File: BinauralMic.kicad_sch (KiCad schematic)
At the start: 0 parts

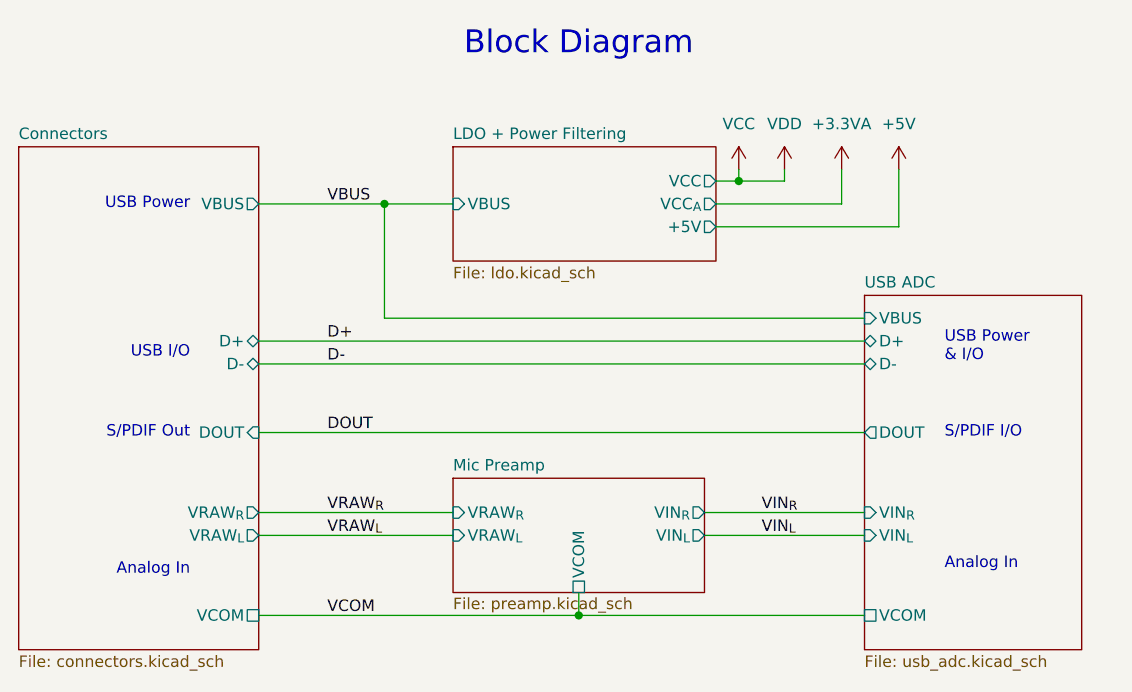
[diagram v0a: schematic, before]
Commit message: Redid schematic and component values according to new recalculations
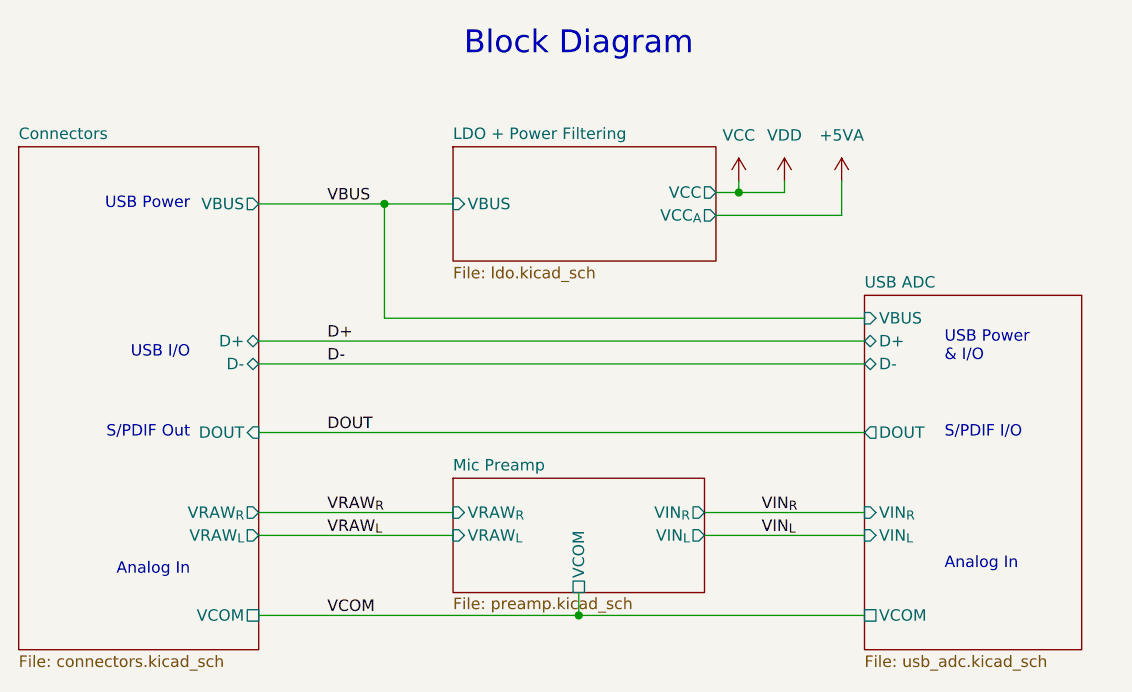
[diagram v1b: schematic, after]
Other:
- sheet LDO + Power Filtering ports: added none; removed +5V
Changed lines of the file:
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@@
 	(title_block
 		(title "Binaural Mic (Block Diagram)")
-		(date "2024-09-15")
-		(rev "1")
+		(date "2025-07-06")
+		(rev "2")
 		(company "Tachyon PCBAs")
-		(comment 1 "first try surely")
+		(comment 1 "second try surely")
 	)
 	(text "Analog In"
@@
 	)
 	(junction
-		(at 121.92 41.91)
+		(at 121.92 43.18)
 		(diameter 0)
 		(color 0 0 0 0)
@@
 	(wire
 		(pts
-			(xy 119.38 44.45) (xy 133.35 44.45)
+			(xy 119.38 45.72) (xy 133.35 45.72)
 		)
 		(stroke
@@
 	(wire
 		(pts
-			(xy 121.92 41.91) (xy 119.38 41.91)
-		)
-		(stroke
-			(width 0)
-			(type default)
-		)
-	)
-	(wire
-		(pts
-			(xy 127 41.91) (xy 121.92 41.91)
+			(xy 121.92 43.18) (xy 119.38 43.18)
+		)
+		(stroke
+			(width 0)
+			(type default)
+		)
+	)
+	(wire
+		(pts
+			(xy 127 43.18) (xy 121.92 43.18)
 		)
 		(stroke
@@
 	(wire
 		(pts
-			(xy 127 40.64) (xy 127 41.91)
+			(xy 127 41.91) (xy 127 43.18)
 		)
 		(stroke
@@
 	(wire
 		(pts
-			(xy 133.35 40.64) (xy 133.35 44.45)
+			(xy 133.35 41.91) (xy 133.35 45.72)
 		)
 		(stroke
@@
 	(wire
 		(pts
-			(xy 139.7 46.99) (xy 119.38 46.99)
-		)
-		(stroke
-			(width 0)
-			(type default)
-		)
-	)
-	(wire
-		(pts
 			(xy 82.55 44.45) (xy 90.17 44.45)
 		)
@@
 	(wire
 		(pts
-			(xy 139.7 40.64) (xy 139.7 46.99)
-		)
-		(stroke
-			(width 0)
-			(type default)
-		)
-	)
-	(wire
-		(pts
-			(xy 121.92 40.64) (xy 121.92 41.91)
+			(xy 121.92 41.91) (xy 121.92 43.18)
 		)
 		(stroke
@@
 	(symbol
 		(lib_id "power:VDD")
-		(at 127 40.64 0)
+		(at 127 41.91 0)
 		(mirror y)
 		(unit 1)
@@
 		(dnp no)
 		(property "Reference" "#PWR02"
-			(at 127 44.45 0)
+			(at 127 45.72 0)
 			(effects
 				(font
@@
 		)
 		(property "Value" "VDD"
-			(at 127 35.56 0)
+			(at 127 36.83 0)
 			(effects
 				(font
@@
 		)
 		(property "Footprint" ""
-			(at 127 40.64 0)
+			(at 127 41.91 0)
 			(effects
 				(font
@@
 		)
 		(property "Datasheet" ""
-			(at 127 40.64 0)
+			(at 127 41.91 0)
 			(effects
 				(font
@@
 		)
 		(property "Description" "Power symbol creates a global label with name \"VDD\""
-			(at 127 40.64 0)
+			(at 127 41.91 0)
 			(effects
 				(font
@@
 	)
 	(symbol
-		(lib_id "power:+3.3VA")
-		(at 133.35 40.64 0)
-		(unit 1)
-		(exclude_from_sim no)
-		(in_bom yes)
-		(on_board yes)
-		(dnp no)
-		(fields_autoplaced yes)
-		(property "Reference" "#PWR031"
-			(at 133.35 44.45 0)
-			(effects
-				(font
-					(size 1.27 1.27)
-				)
-				(hide yes)
-			)
-		)
-		(property "Value" "+3.3VA"
-			(at 133.35 35.56 0)
-			(effects
-				(font
-					(size 1.27 1.27)
-				)
-			)
-		)
-		(property "Footprint" ""
-			(at 133.35 40.64 0)
-			(effects
-				(font
-					(size 1.27 1.27)
-				)
-				(hide yes)
-			)
-		)
-		(property "Datasheet" ""
-			(at 133.35 40.64 0)
-			(effects
-				(font
-					(size 1.27 1.27)
-				)
-				(hide yes)
-			)
-		)
-		(property "Description" "Power symbol creates a global label with name \"+3.3VA\""
-			(at 133.35 40.64 0)
-			(effects
-				(font
-					(size 1.27 1.27)
-				)
-				(hide yes)
-			)
-		)
-		(pin "1"
-		)
-		(instances
-			(project "BinauralMic"
-				(path "/d9e790b9-8aa4-4e58-8bd7-6ef4bc890627"
-					(reference "#PWR031")
-					(unit 1)
-				)
-			)
-		)
-	)
-	(symbol
-		(lib_id "power:+5V")
-		(at 139.7 40.64 0)
+		(lib_id "power:+5VA")
+		(at 133.35 41.91 0)
 		(unit 1)
 		(exclude_from_sim no)
@@
 		(fields_autoplaced yes)
 		(property "Reference" "#PWR03"
-			(at 139.7 44.45 0)
-			(effects
-				(font
-					(size 1.27 1.27)
-				)
-				(hide yes)
-			)
-		)
-		(property "Value" "+5V"
-			(at 139.7 35.56 0)
+			(at 133.35 45.72 0)
+			(effects
+				(font
+					(size 1.27 1.27)
+				)
+				(hide yes)
+			)
+		)
+		(property "Value" "+5VA"
+			(at 133.35 36.83 0)
 			(effects
 				(font
@@
 		)
 		(property "Footprint" ""
-			(at 139.7 40.64 0)
+			(at 133.35 41.91 0)
 			(effects
 				(font
@@
 		)
 		(property "Datasheet" ""
-			(at 139.7 40.64 0)
-			(effects
-				(font
-					(size 1.27 1.27)
-				)
-				(hide yes)
-			)
-		)
-		(property "Description" "Power symbol creates a global label with name \"+5V\""
-			(at 139.7 40.64 0)
+			(at 133.35 41.91 0)
+			(effects
+				(font
+					(size 1.27 1.27)
+				)
+				(hide yes)
+			)
+		)
+		(property "Description" "Power symbol creates a global label with name \"+5VA\""
+			(at 133.35 41.91 0)
 			(effects
 				(font
@@
 		)
 		(instances
-			(project "BinauralMic"
+			(project ""
 				(path "/d9e790b9-8aa4-4e58-8bd7-6ef4bc890627"
 					(reference "#PWR03")
@@
 	(symbol
 		(lib_id "power:VCC")
-		(at 121.92 40.64 0)
+		(at 121.92 41.91 0)
 		(unit 1)
 		(exclude_from_sim no)
@@
 		(fields_autoplaced yes)
 		(property "Reference" "#PWR01"
-			(at 121.92 44.45 0)
+			(at 121.92 45.72 0)
 			(effects
 				(font
@@
 		)
 		(property "Value" "VCC"
-			(at 121.92 35.56 0)
+			(at 121.92 36.83 0)
 			(effects
 				(font
@@
 		)
 		(property "Footprint" ""
-			(at 121.92 40.64 0)
+			(at 121.92 41.91 0)
 			(effects
 				(font
@@
 		)
 		(property "Datasheet" ""
-			(at 121.92 40.64 0)
+			(at 121.92 41.91 0)
 			(effects
 				(font
@@
 		)
 		(property "Description" "Power symbol creates a global label with name \"VCC\""
-			(at 121.92 40.64 0)
+			(at 121.92 41.91 0)
 			(effects
 				(font
@@
 		)
 		(pin "VCC" output
-			(at 119.38 41.91 0)
+			(at 119.38 43.18 0)
 			(effects
 				(font
@@
 		)
 		(pin "VCC_{A}" output
-			(at 119.38 44.45 0)
-			(effects
-				(font
-					(size 1.27 1.27)
-				)
-				(justify right)
-			)
-		)
-		(pin "+5V" output
-			(at 119.38 46.99 0)
-			(effects
-				(font
+			(at 119.38 45.72 0)
+			(effects
+				(font
